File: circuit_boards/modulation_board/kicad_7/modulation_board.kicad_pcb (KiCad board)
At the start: 4 copper layers, 111.8 x 165.1 mm, 243 parts, among them J1 MOD_BOARD_EXT_CON, J2 VCO_BOARD_CON, J3 VCF_BOARD_CON, J301 SWD_header, J4 power_entry, Q501 MMBT3904, Q801 MMBT3904, SW301 5511M12, SW501 E-Switch_EG2301B, SW502 E-Switch_EG2301B, SW503 E-Switch_EG2301B, SW504 E-Switch_EG2301B, SW505 E-Switch_EG2301B, SW506 E-Switch_EG2301B, SW507 E-Switch_EG2301B, SW801 E-Switch_EG2301B, SW802 SR1712F-0204, U1 STM32L412K8Ux, U10 TL072, U1001 L78L05_SOT89, U1002 L79L05_SOT89, U1003 L78L33_SOT89, U11 74HC595, U12 SSI2130, U13 TL072, U14 TL072, U15 MCP6002-xSN, U2 VO0600T, U3 SN74LV1T34DBV, U4 LM4040C-2.5, U5 74HC4067PW, U6 74HC4067PW, U7 MCP6002-xSN, U8 DAC8162xDGSx, U801 LM4040C-2.5, U9 DAC128S085CIMT, Y301 32_768KHZ

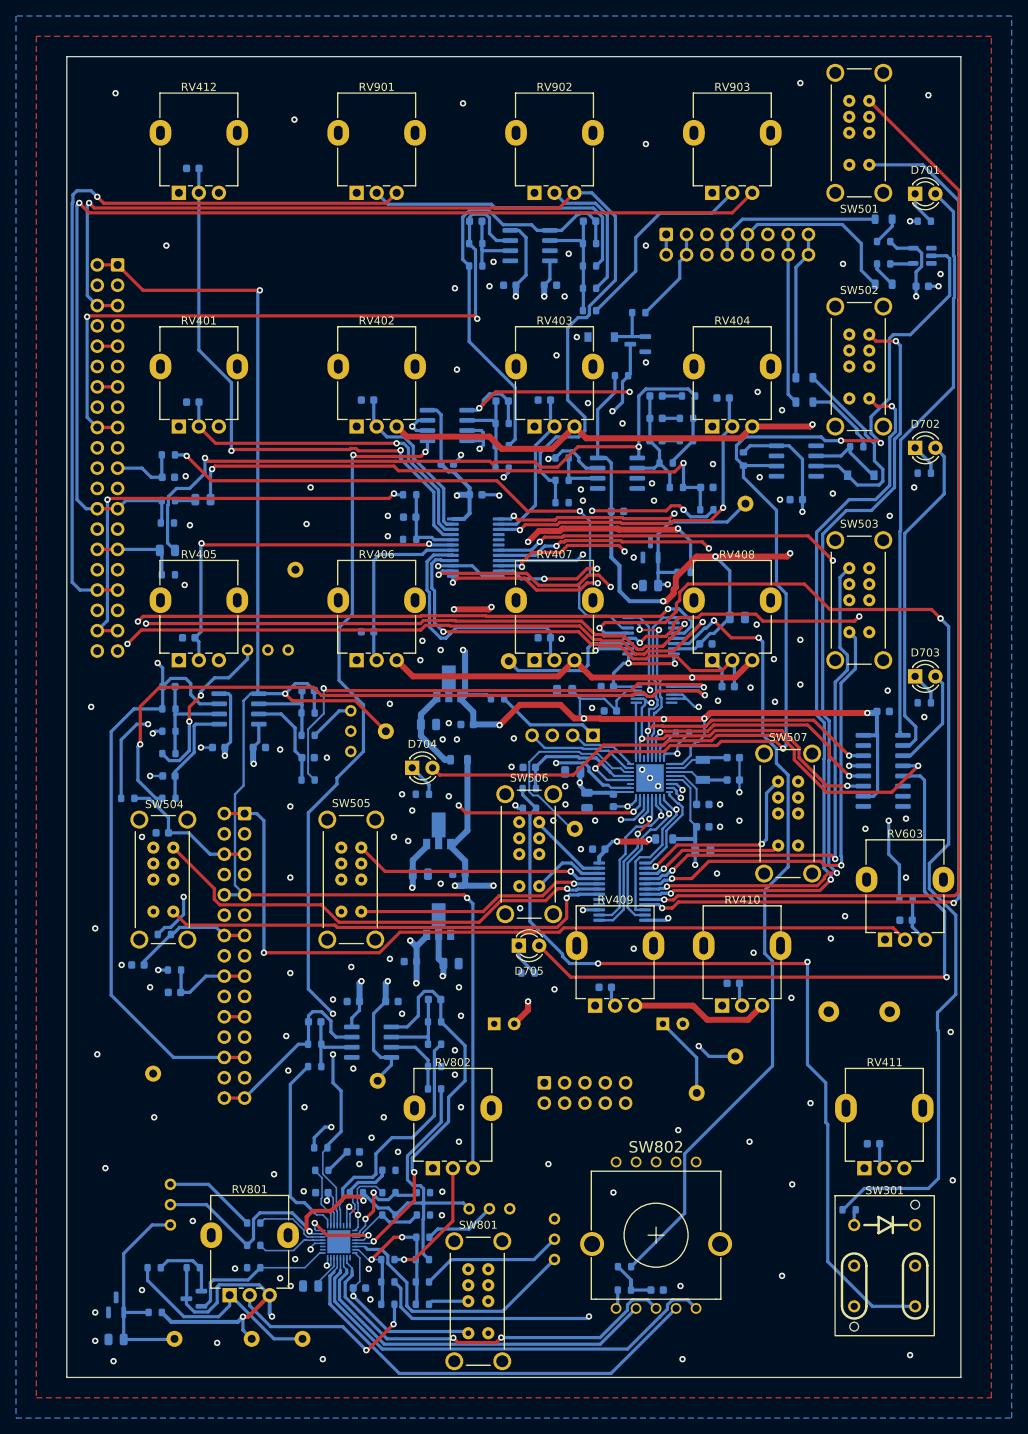
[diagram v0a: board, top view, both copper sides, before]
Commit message: Update PCBs, tweak vals, add VCF CV from DAC
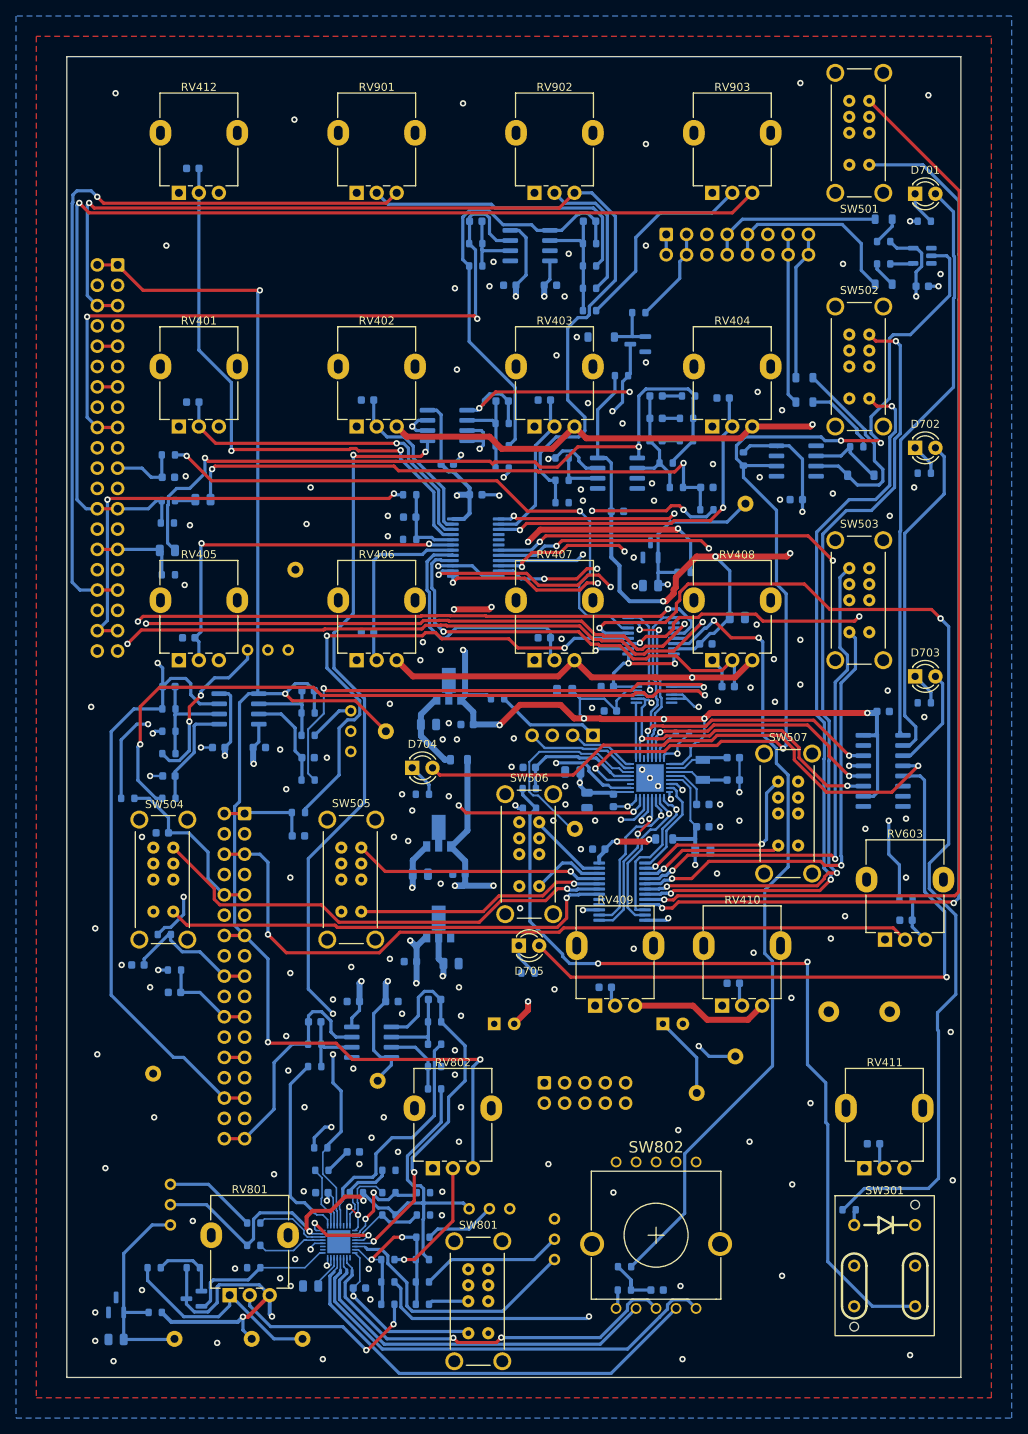
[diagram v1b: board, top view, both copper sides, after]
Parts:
- removed TP604: CH_H, TestPoint:TestPoint_Keystone_5000-5004_Miniature
- added C619: 100n, Capacitor_SMD:C_0603_1608Metric, B.Cu at (70.9, 120.3)
- added R618: 1k, Resistor_SMD:R_0603_1608Metric, B.Cu at (70.9, 117.3)
- J3: footprint custom_footprints:30_pin_IDC-Header -> custom_footprints:34_pin_IDC_header
- R903: value 22k -> 20k
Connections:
- net /digital_ctl_generators/MIDI_MOD_WHEEL renamed /digital_ctl_generators/MODOSC_AMP_CTL
- J3 pad 1: /VOLUME_CV -> /VCF_FREQ_CV
- J3 pad 10: /PITCH_CV -> /VCA_ENV
- J3 pad 13: /FEEDBACK_CV -> /PITCH_CV
- J3 pad 14: /FEEDBACK_CV -> /PITCH_CV
- J3 pad 17: /VCF_ENV -> /FEEDBACK_CV
- J3 pad 18: /VCF_ENV -> /FEEDBACK_CV
- J3 pad 2: /VOLUME_CV -> /VCF_FREQ_CV
- J3 pad 21: /S_AND_H_MIXER -> /VCF_ENV
- J3 pad 22: /S_AND_H_MIXER -> /VCF_ENV
- J3 pad 25: /S_AND_H -> /S_AND_H_MIXER
- J3 pad 26: /S_AND_H -> /S_AND_H_MIXER
- J3 pad 29: /MOD_OSC -> /S_AND_H
- J3 pad 30: /MOD_OSC -> /S_AND_H
- J3 pad 5: /VCA_ENV -> /VOLUME_CV
- J3 pad 6: /VCA_ENV -> /VOLUME_CV
- J3 pad 9: /PITCH_CV -> /VCA_ENV
- R607 pad 1: Net-(R607-Pad1) -> Net-(U9-VOUT_H)
- U1 pad 7: /digital_ctl_generators/analog_controls/POT_MUX.COM_ANALOG -> /digital_ctl_generators/analog_controls/POT_MUX.COM_DISCRETE
- U1 pad 8: /digital_ctl_generators/analog_controls/POT_MUX.COM_DISCRETE -> /digital_ctl_generators/analog_controls/POT_MUX.COM_ANALOG
- U9 pad 12: Net-(R607-Pad1) -> Net-(R618-Pad1)
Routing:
- net Net-(R607-Pad1): track 68.9 -> 0.00 mm, vias 3 -> 0
- net Net-(R618-Pad1): track 0.00 -> 66.2 mm, vias 0 -> 2
- net Net-(U9-VOUT_H): track 18.1 -> 68.7 mm, vias 0 -> 3
- net /VCF_FREQ_CV: track 0.00 -> 11.4 mm
- net /MOD_OSC: track 133.8 -> 141.5 mm
- net /VOLUME_CV: track 103.9 -> 97.4 mm
- net /S_AND_H: track 196.6 -> 200.6 mm
- net /VCA_ENV: track 17.8 -> 21.8 mm
- net /S_AND_H_MIXER: track 176.5 -> 178.6 mm
- net /digital_ctl_generators/analog_controls/POT_MUX.COM_ANALOG: track 64.8 -> 63.0 mm
- net /FEEDBACK_CV: track 15.3 -> 16.9 mm
- net /PITCH_CV: track 189.4 -> 188.6 mm, vias 3 -> 4
- net /digital_ctl_generators/analog_controls/POT_MUX.COM_DISCRETE: track 12.0 -> 12.7 mm
- net Net-(U12A-square_out): track 115.5 -> 116.1 mm
- net /digital_ctl_generators/DAC/DAC_SPI.SDO: track 52.7 -> 52.1 mm
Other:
- board text added: "MICRO-OX Modulation Board rev 0 2023-04-25"
- board text removed: "MICRO-OX Modulation Board rev 0 2023-04-21"

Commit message: Resistor tweaks while evaluating 1st build
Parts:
- R701, R702, R703, R704, R705: value 390 -> 4k7
- R806: value 100k -> 51k
- R903: value 20k -> 10k
